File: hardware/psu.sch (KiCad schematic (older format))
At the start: 18 parts, among them CON401 BARREL_JACK, U401 NCP3170-D

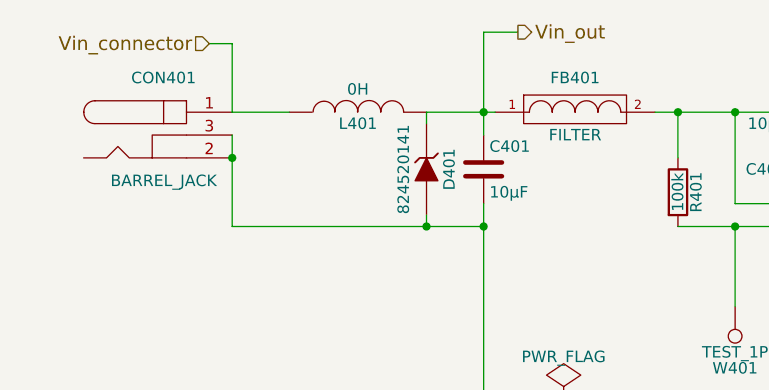
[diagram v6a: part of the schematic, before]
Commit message: Fixed some bugs and annotated rest of the footprints
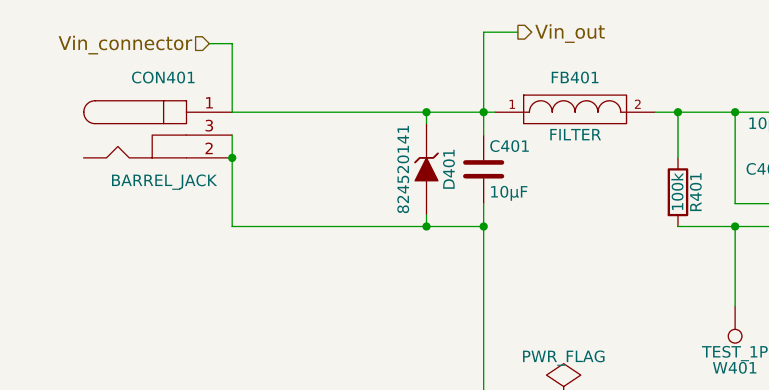
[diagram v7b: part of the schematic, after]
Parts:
- removed L401: 0H, symbol INDUCTOR
- C401, C402, C403, C404, C405: footprint Capacitors_SMD:C_0805 -> Capacitors_SMD:C_0805_HandSoldering
- CON401: footprint (none) -> Connect:BARREL_JACK
- D402: footprint (none) -> dodekaedri:Micro_SMP
- FB401, FB402: footprint (none) -> Resistors_SMD:R_0805_HandSoldering
- L402: footprint (none) -> dodekaedri:psu_ind
- U401: footprint (none) -> Housings_SOIC:SOIC-8_3.9x4.9mm_Pitch1.27mm
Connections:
- net Vin_out is gone; now on net Vin_connector: C401.1, D401.1 (K), FB401.1
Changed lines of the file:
@@
 F 0 "U401" H 5800 3650 60  0000 C CNN
 F 1 "NCP3170-D" H 5700 3800 60  0000 C CNN
-F 2 "" H 5450 3450 60  0001 C CNN
+F 2 "Housings_SOIC:SOIC-8_3.9x4.9mm_Pitch1.27mm" H 5450 3450 60  0001 C CNN
 F 3 "" H 5450 3450 60  0001 C CNN
 	1    5450 3450
@@
 F 0 "C403" H 4825 3800 50  0000 L CNN
 F 1 "6n8" H 4825 3600 50  0000 L CNN
-F 2 "Capacitors_SMD:C_0805" H 4838 3550 50  0001 C CNN
+F 2 "Capacitors_SMD:C_0805_HandSoldering" H 4838 3550 50  0001 C CNN
 F 3 "" H 4800 3700 50  0000 C CNN
 	1    4800 3700
@@
 F 0 "C402" H 4725 3200 50  0000 L CNN
 F 1 "10µF" H 4725 3000 50  0000 L CNN
-F 2 "Capacitors_SMD:C_0805" H 4738 2950 50  0001 C CNN
+F 2 "Capacitors_SMD:C_0805_HandSoldering" H 4738 2950 50  0001 C CNN
 F 3 "" H 4700 3100 50  0000 C CNN
 	1    4700 3100
@@
 F 0 "C404" H 7025 3850 50  0000 L CNN
 F 1 "10µF" H 7025 3650 50  0000 L CNN
-F 2 "Capacitors_SMD:C_0805" H 7038 3600 50  0001 C CNN
+F 2 "Capacitors_SMD:C_0805_HandSoldering" H 7038 3600 50  0001 C CNN
 F 3 "" H 7000 3750 50  0000 C CNN
 	1    7000 3750
@@
 F 0 "L402" V 6200 3350 50  0000 C CNN
 F 1 "100µH" V 6350 3350 50  0000 C CNN
-F 2 "" H 6250 3350 50  0001 C CNN
+F 2 "dodekaedri:psu_ind" H 6250 3350 50  0001 C CNN
 F 3 "" H 6250 3350 50  0000 C CNN
 	1    6250 3350
@@
 Connection ~ 5450 4200
 $Comp
-L GND #PWR401
+L GND #PWR018
 U 1 1 57E32388
 P 5450 4300
-F 0 "#PWR401" H 5450 4050 50  0001 C CNN
+F 0 "#PWR018" H 5450 4050 50  0001 C CNN
 F 1 "GND" H 5450 4150 50  0000 C CNN
 F 2 "" H 5450 4300 50  0000 C CNN
@@
 F 0 "CON401" H 1950 3300 50  0000 C CNN
 F 1 "BARREL_JACK" H 1950 2850 50  0000 C CNN
-F 2 "" H 1950 3050 50  0001 C CNN
+F 2 "Connect:BARREL_JACK" H 1950 3050 50  0001 C CNN
 F 3 "" H 1950 3050 50  0000 C CNN
 	1    1950 3050
@@
 F 0 "C401" H 3375 3300 50  0000 L CNN
 F 1 "10µF" H 3375 3100 50  0000 L CNN
-F 2 "Capacitors_SMD:C_0805" H 3388 3050 50  0001 C CNN
+F 2 "Capacitors_SMD:C_0805_HandSoldering" H 3388 3050 50  0001 C CNN
 F 3 "" H 3350 3200 50  0000 C CNN
 	1    3350 3200
@@
 F 0 "C405" H 7825 3850 50  0000 L CNN
 F 1 "10µF" H 7825 3650 50  0000 L CNN
-F 2 "Capacitors_SMD:C_0805" H 7838 3600 50  0001 C CNN
+F 2 "Capacitors_SMD:C_0805_HandSoldering" H 7838 3600 50  0001 C CNN
 F 3 "" H 7800 3750 50  0000 C CNN
 	1    7800 3750
@@
 Connection ~ 3350 2950
 $Comp
-L PWR_FLAG #FLG402
+L PWR_FLAG #FLG019
 U 1 1 57E44620
 P 5350 2950
-F 0 "#FLG402" H 5350 3045 50  0001 C CNN
+F 0 "#FLG019" H 5350 3045 50  0001 C CNN
 F 1 "PWR_FLAG" H 5350 3130 50  0000 C CNN
 F 2 "" H 5350 2950 50  0000 C CNN
@@
 Wire Wire Line
 	2150 2650 2250 2650
-$Comp
-L INDUCTOR L401
-U 1 1 57E56F10
-P 2800 2950
-F 0 "L401" V 2750 2950 50  0000 C CNN
-F 1 "0H" V 2900 2950 50  0000 C CNN
-F 2 "" H 2800 2950 50  0001 C CNN
-F 3 "" H 2800 2950 50  0000 C CNN
-	1    2800 2950
-	0    -1   -1   0
-$EndComp
-Wire Wire Line
-	3100 2950 3400 2950
+Wire Wire Line
+	2250 2950 3400 2950
 Wire Wire Line
 	3350 2600 3350 3050
@@
 Connection ~ 3100 3450
 Wire Wire Line
-	2250 2950 2500 2950
-Wire Wire Line
 	3350 3350 3350 4200
 Text HLabel 3500 2600 2    60   Output ~ 0
@@
 F 0 "FB401" H 3750 3100 50  0000 C CNN
 F 1 "FILTER" H 3750 2850 50  0000 C CNN
-F 2 "" H 3750 2950 50  0001 C CNN
+F 2 "Resistors_SMD:R_0805_HandSoldering" H 3750 2950 50  0001 C CNN
 F 3 "" H 3750 2950 50  0000 C CNN
 	1    3750 2950
@@
 F 0 "FB402" H 7400 3500 50  0000 C CNN
 F 1 "FILTER" H 7400 3250 50  0000 C CNN
-F 2 "" H 7400 3350 50  0001 C CNN
+F 2 "Resistors_SMD:R_0805_HandSoldering" H 7400 3350 50  0001 C CNN
 F 3 "" H 7400 3350 50  0000 C CNN
 	1    7400 3350
@@
 F 0 "D402" H 8150 3850 50  0000 C CNN
 F 1 "MSP3V3" H 8150 3650 50  0000 C CNN
-F 2 "" H 8150 3750 50  0001 C CNN
+F 2 "dodekaedri:Micro_SMP" H 8150 3750 50  0001 C CNN
 F 3 "" H 8150 3750 50  0000 C CNN
 	1    8150 3750
@@
 	2250 2650 2250 2950
 $Comp
-L PWR_FLAG #FLG401
+L PWR_FLAG #FLG020
 U 1 1 57EE5195
 P 3700 4200
-F 0 "#FLG401" H 3700 4295 50  0001 C CNN
+F 0 "#FLG020" H 3700 4295 50  0001 C CNN
 F 1 "PWR_FLAG" H 3700 4380 50  0000 C CNN
 F 2 "" H 3700 4200 50  0000 C CNN
@@
 $EndComp
 Connection ~ 3700 4200
+Connection ~ 3100 2950
 $EndSCHEMATC
